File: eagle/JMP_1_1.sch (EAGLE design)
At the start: 16 parts, among them X1 Out B, X2 Out B, X3 Out A, X4 Out A, X5 USB-MB-H, X6 USB-MICROB

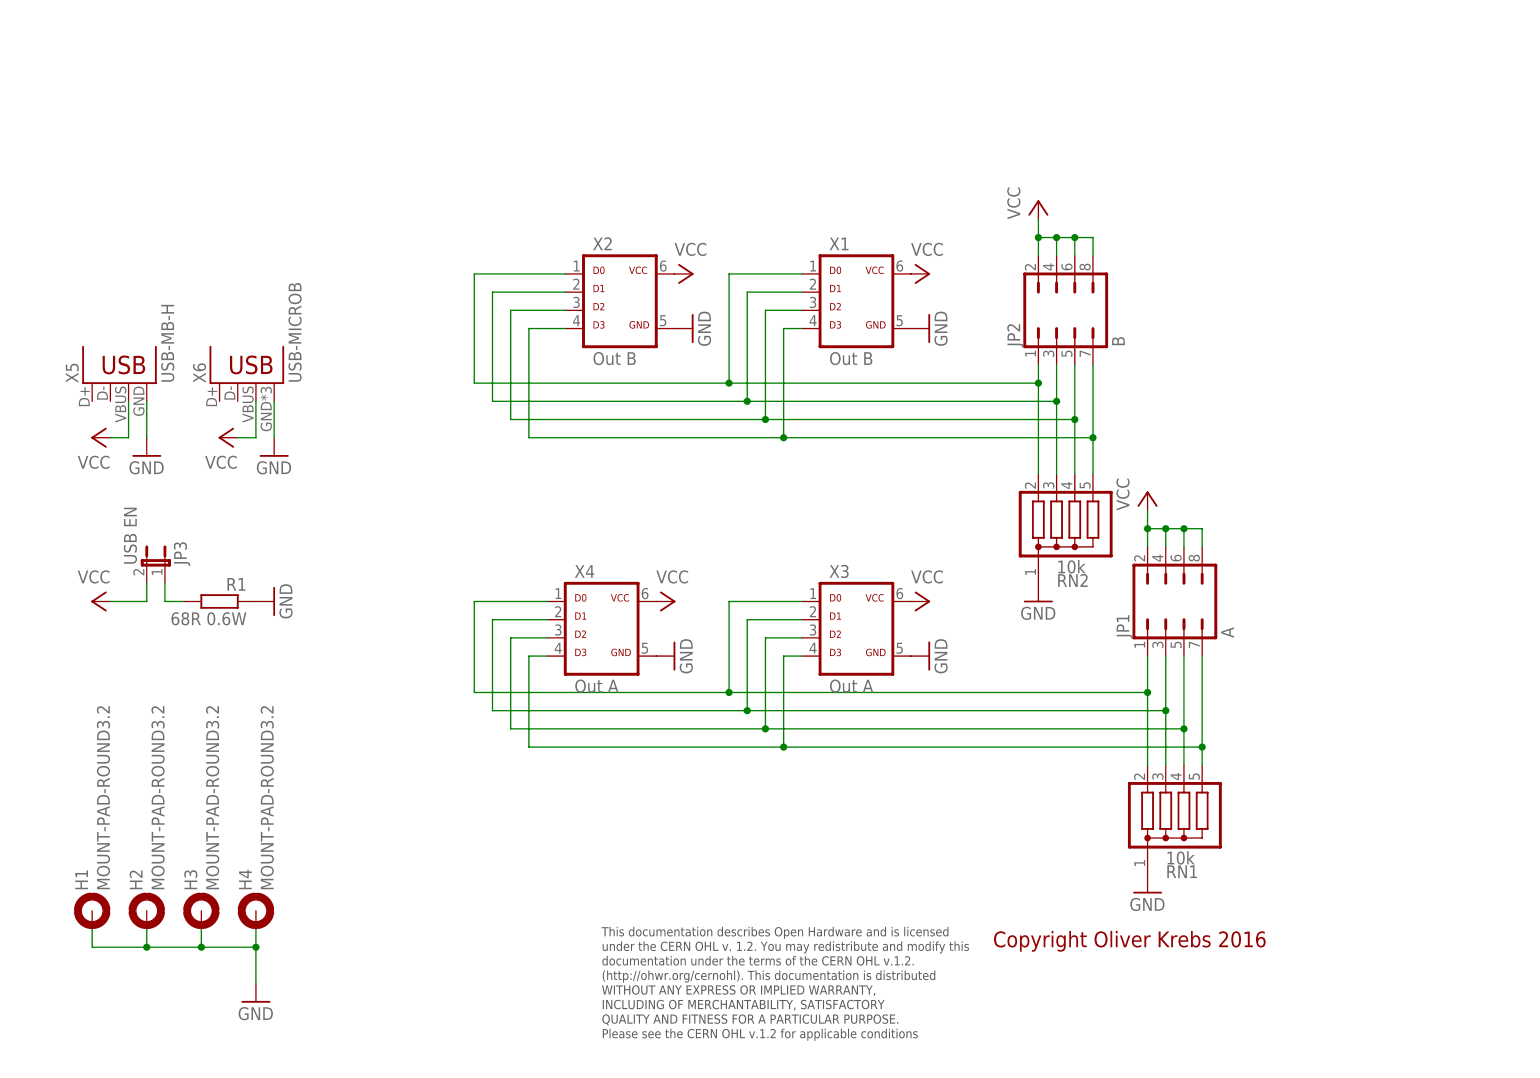
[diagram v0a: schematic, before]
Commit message: Add new tetra-Board and arduino files
Add AMP_1_0, AVC_1_0, D18_1_1, IOP_1_2, MIC_1_0, PIN_1_1, POT_1_0, PWA_1_0, PWR_1_0, RGF 2.0, SOC_2_0, VLT_1_0
Add mex_nano_shield_keyboard, mex_nano_shied_numbers

New arduino projects
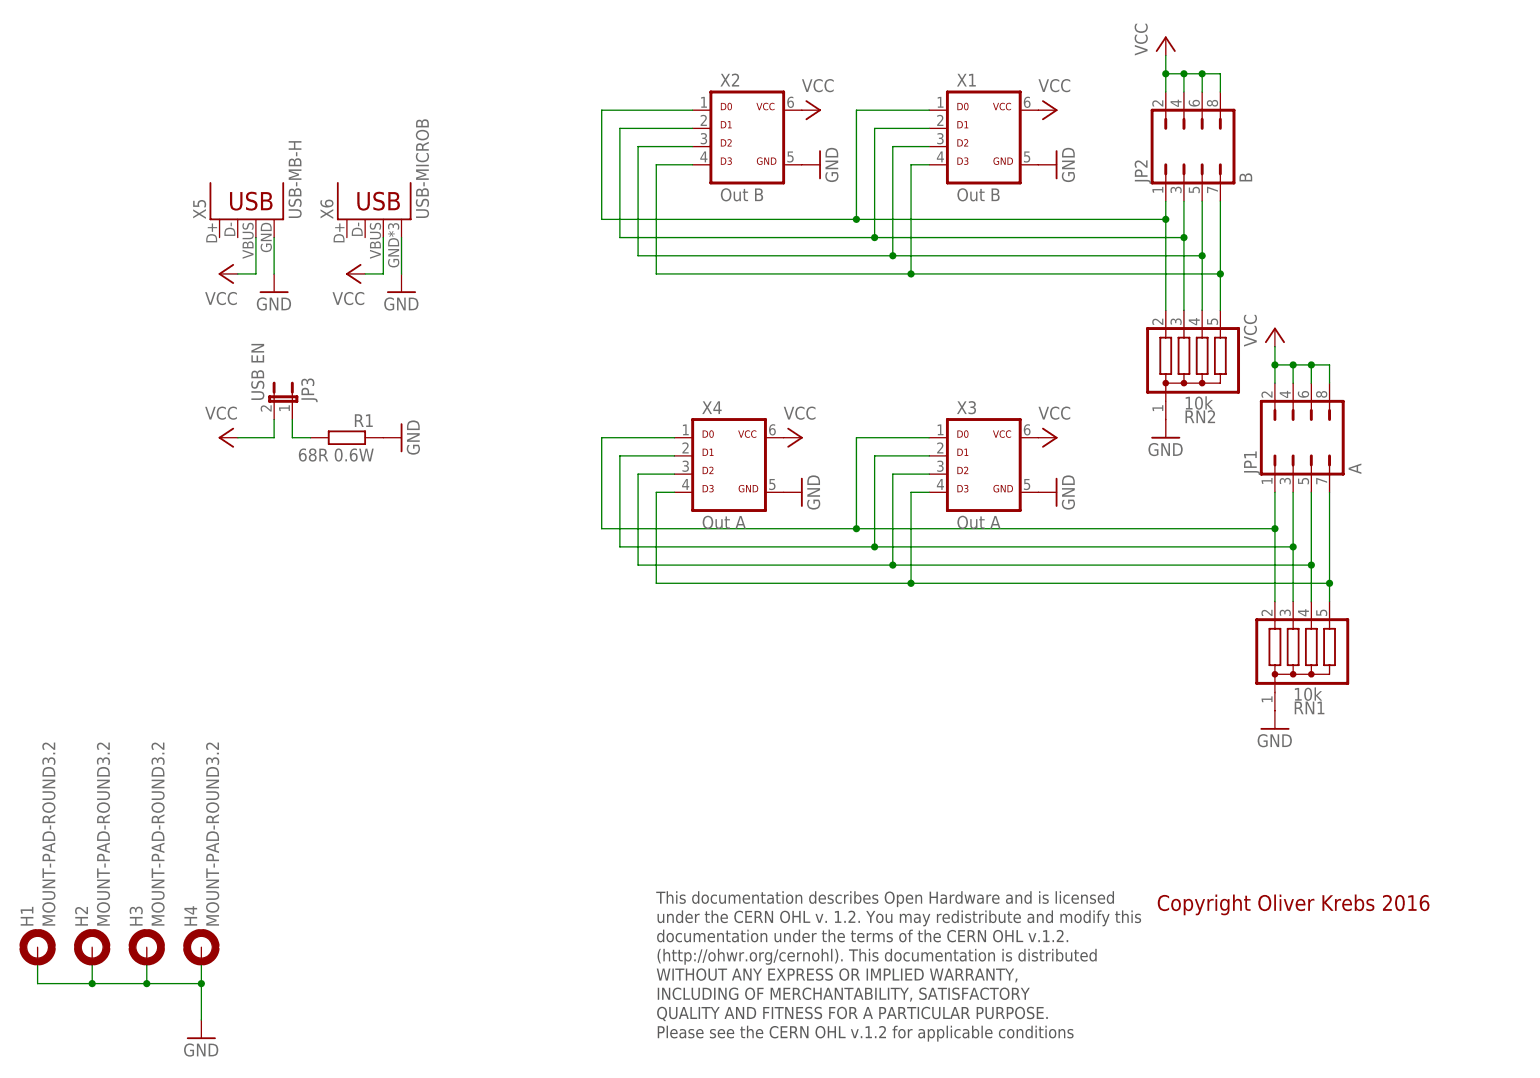
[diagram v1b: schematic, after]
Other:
- moved on the sheet: H1, H2, H3, H4, JP1, JP2, JP3, R1, RN1, RN2, X1, X2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
